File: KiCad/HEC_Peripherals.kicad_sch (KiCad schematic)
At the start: 17 parts, among them J2 Conn_02x12_Odd_Even, J6 DE9_Plug_MountingHoles, J7 AudioJack3, J8 NES_Port_Male, U43 74LS06, U44 74LS541, Y1 Crystal

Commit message: Preliminary routing
Changed footprint pad size to allow 2 traces to be routed between adjacent pads. Finished routing all ICs. Bypass caps not added. Some traces may need to be optimized.
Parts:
- U42: footprint Package_DIP:DIP-40_W15.24mm_Socket -> Library:DIP-40_W15.24mm_Socket_ThinPads
- U43: footprint Package_DIP:DIP-14_W7.62mm_Socket -> Library:DIP-14_W7.62mm_Socket_ThinPads
- U44: footprint Package_DIP:DIP-20_W7.62mm_Socket -> Library:DIP-20_W7.62mm_Socket_ThinPads
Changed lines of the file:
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@@
       (effects (font (size 1.27 1.27)))
     )
-    (property "Footprint" "Package_DIP:DIP-14_W7.62mm_Socket" (at 223.52 104.14 0)
+    (property "Footprint" "Library:DIP-14_W7.62mm_Socket_ThinPads" (at 223.52 104.14 0)
       (effects (font (size 1.27 1.27)) hide)
     )
@@
       (effects (font (size 1.27 1.27)))
     )
-    (property "Footprint" "Package_DIP:DIP-14_W7.62mm_Socket" (at 138.43 83.82 0)
+    (property "Footprint" "Library:DIP-14_W7.62mm_Socket_ThinPads" (at 138.43 83.82 0)
       (effects (font (size 1.27 1.27)) hide)
     )
@@
       (effects (font (size 1.27 1.27)))
     )
-    (property "Footprint" "Package_DIP:DIP-14_W7.62mm_Socket" (at 223.52 91.44 0)
+    (property "Footprint" "Library:DIP-14_W7.62mm_Socket_ThinPads" (at 223.52 91.44 0)
       (effects (font (size 1.27 1.27)) hide)
     )
@@
       (effects (font (size 1.27 1.27)) (justify left))
     )
-    (property "Footprint" "Package_DIP:DIP-20_W7.62mm_Socket" (at 94.615 167.64 0)
+    (property "Footprint" "Library:DIP-20_W7.62mm_Socket_ThinPads" (at 94.615 167.64 0)
       (effects (font (size 1.27 1.27)) hide)
     )
@@
       (effects (font (size 1.27 1.27)))
     )
-    (property "Footprint" "Package_DIP:DIP-14_W7.62mm_Socket" (at 223.52 65.405 0)
+    (property "Footprint" "Library:DIP-14_W7.62mm_Socket_ThinPads" (at 223.52 65.405 0)
       (effects (font (size 1.27 1.27)) hide)
     )
@@
       (effects (font (size 1.27 1.27)) (justify right))
     )
-    (property "Footprint" "Package_DIP:DIP-14_W7.62mm_Socket" (at 217.805 135.89 0)
+    (property "Footprint" "Library:DIP-14_W7.62mm_Socket_ThinPads" (at 217.805 135.89 0)
       (effects (font (size 1.27 1.27)) hide)
     )
@@
       (effects (font (size 1.27 1.27)))
     )
-    (property "Footprint" "Package_DIP:DIP-14_W7.62mm_Socket" (at 138.43 68.58 0)
+    (property "Footprint" "Library:DIP-14_W7.62mm_Socket_ThinPads" (at 138.43 68.58 0)
       (effects (font (size 1.27 1.27)) hide)
     )
@@
       (effects (font (size 1.27 1.27)))
     )
-    (property "Footprint" "Package_DIP:DIP-40_W15.24mm_Socket" (at 170.815 76.2 0)
+    (property "Footprint" "Library:DIP-40_W15.24mm_Socket_ThinPads" (at 170.815 76.2 0)
       (effects (font (size 1.27 1.27)) hide)
     )
@@
       (effects (font (size 1.27 1.27)))
     )
-    (property "Footprint" "Package_DIP:DIP-14_W7.62mm_Socket" (at 223.52 78.74 0)
-      (effects (font (size 1.27 1.27)) hide)
-    )
+    (property "Footprint" "Library:DIP-14_W7.62mm_Socket_ThinPads" (at 223.52 78.74 0)
+      (effects (font (size 1.27 1.27)) hide)
+    )

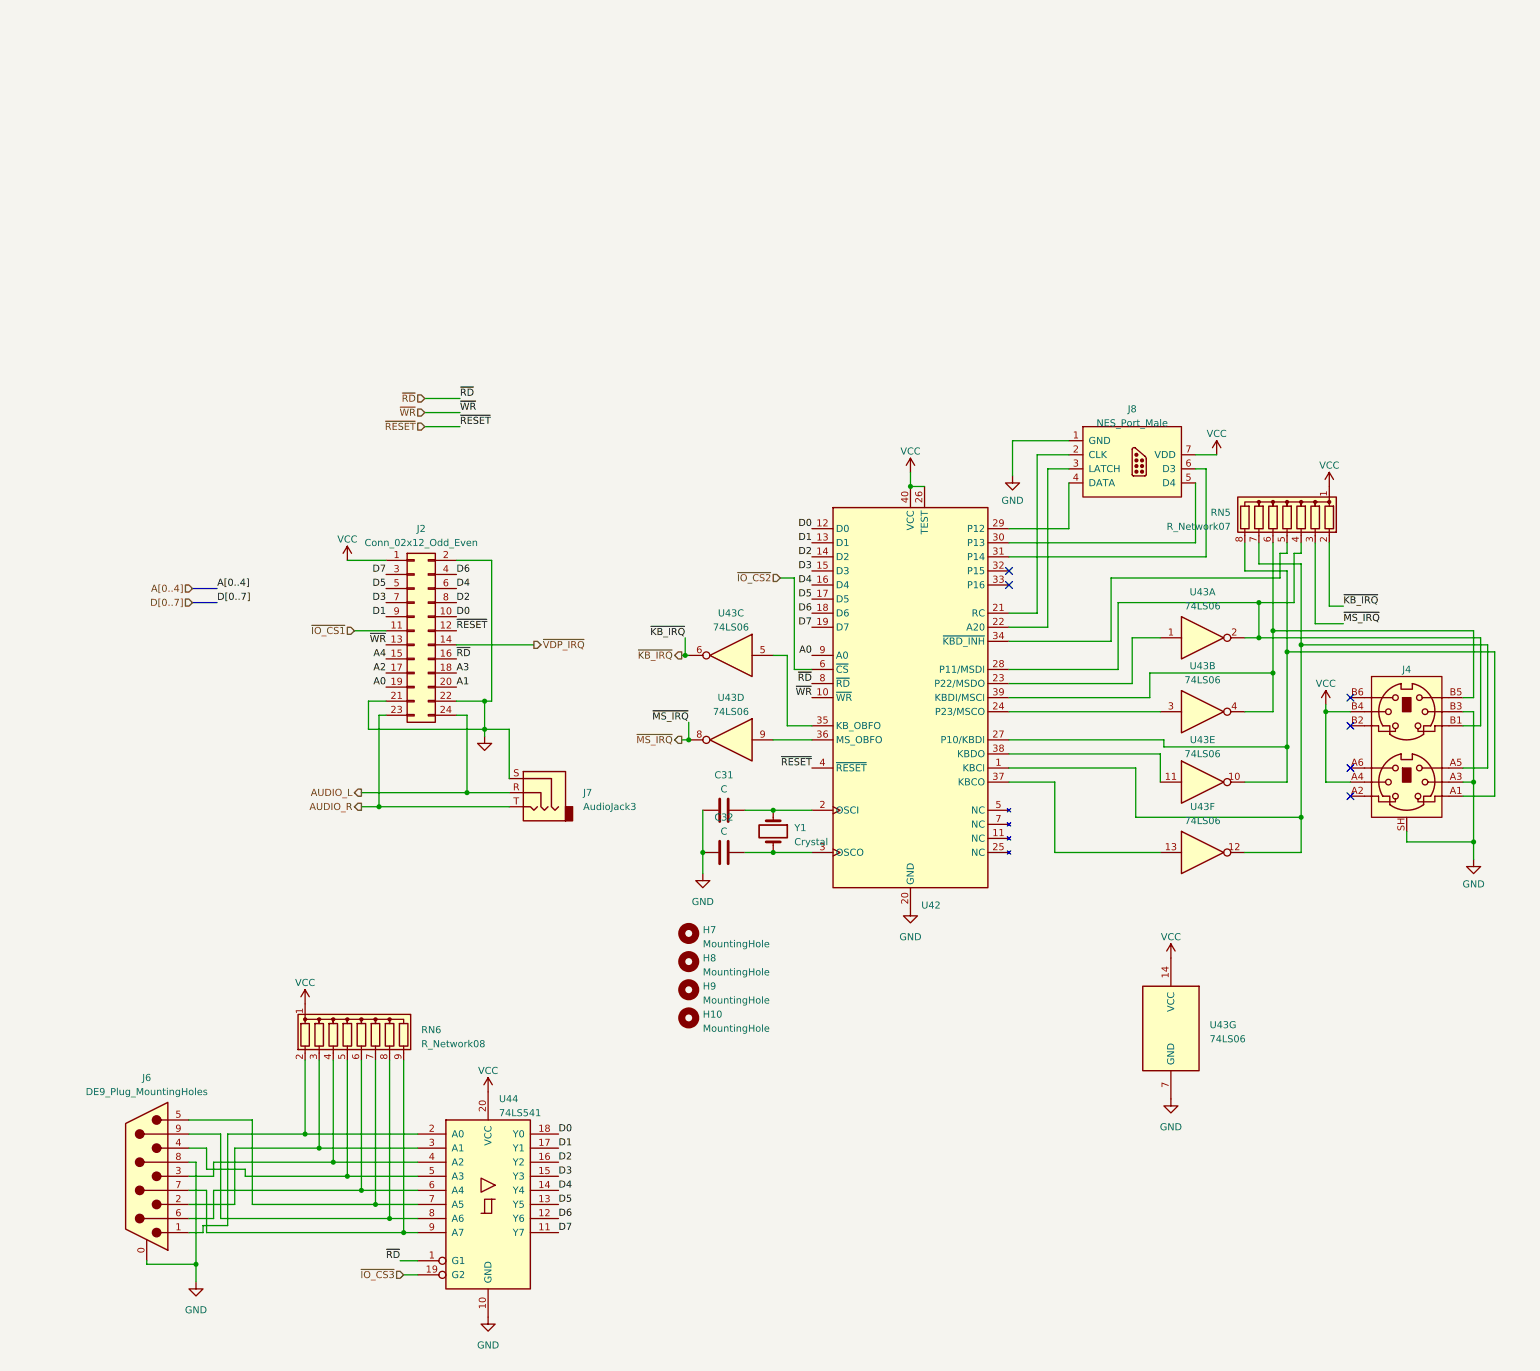
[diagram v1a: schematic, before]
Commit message: Change resistor network, add revision number
Changed most of the resistor network footprints so that they would accept both 9 pin and 5 pin resistor networks (since I bought 50 of those 5 pin ones!). Power routing optimizations. Added a revision number to the silkscreen to distinguish the board
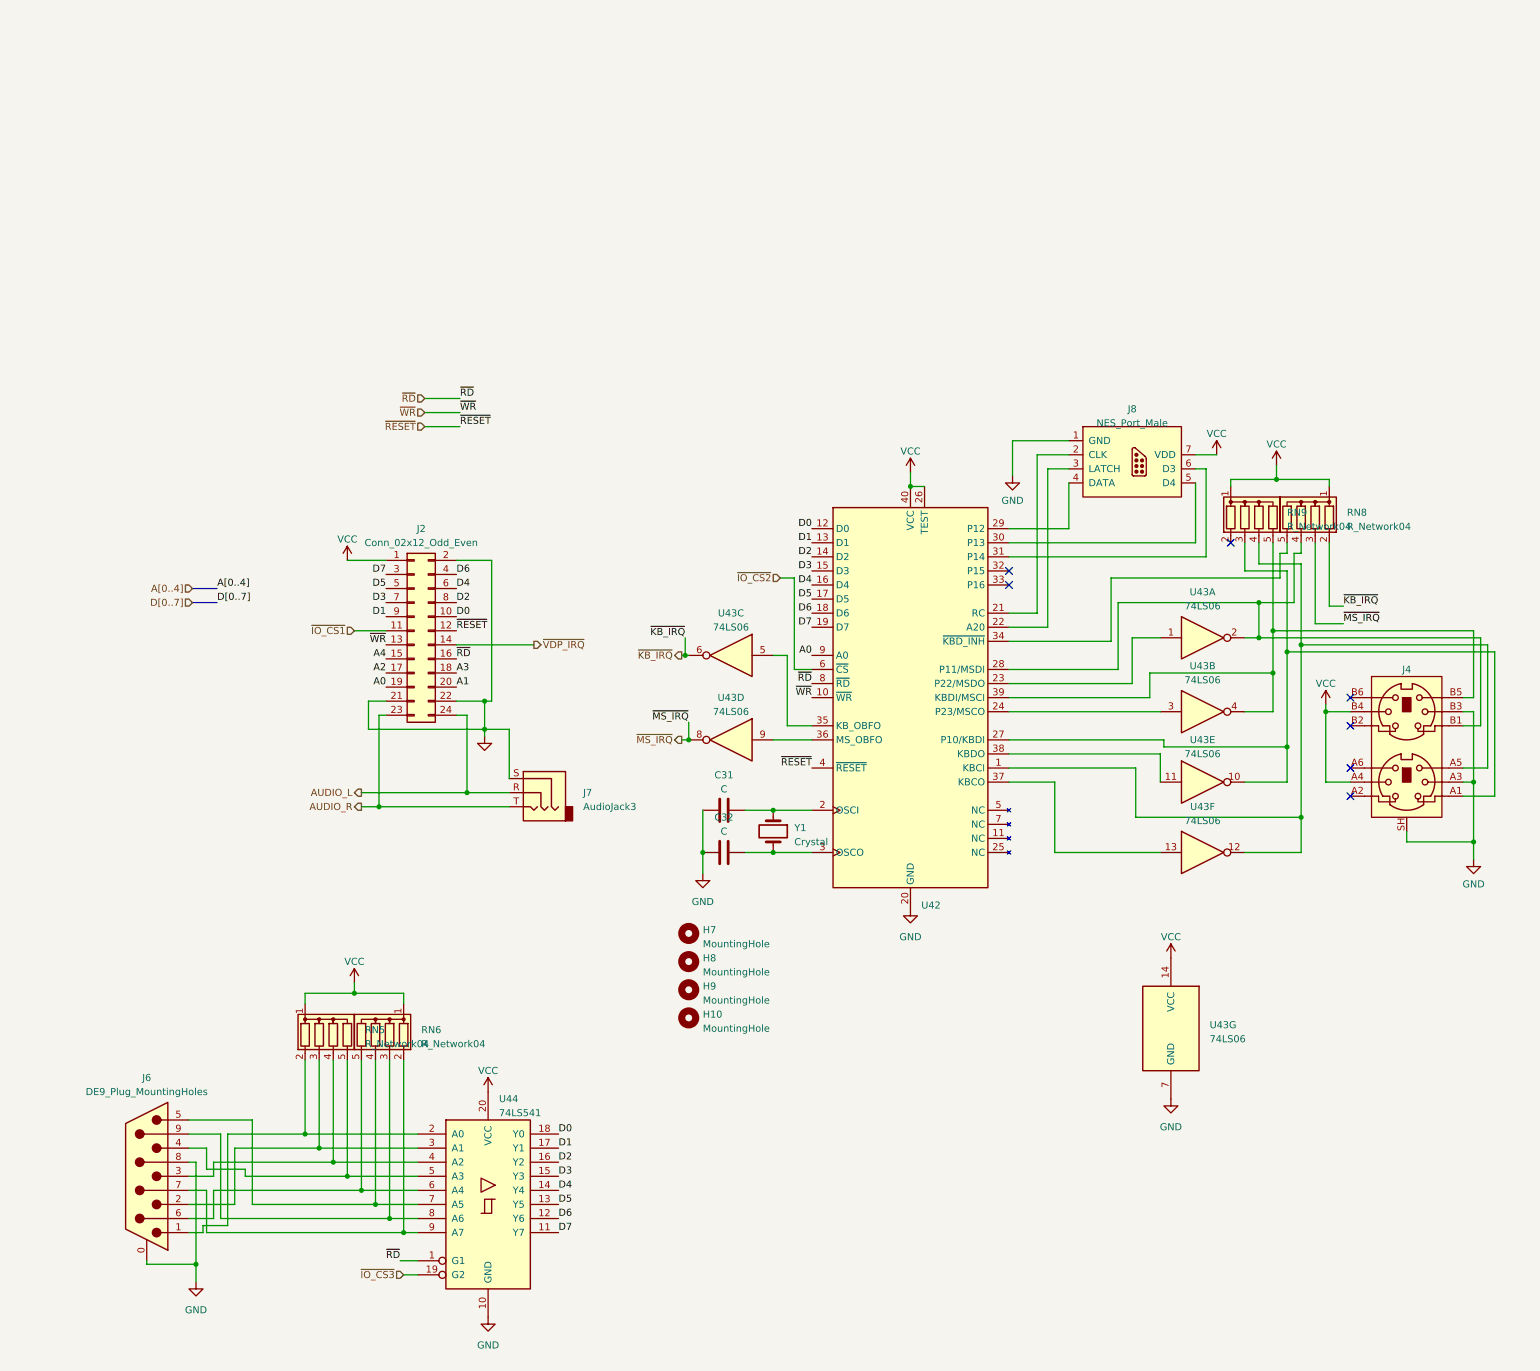
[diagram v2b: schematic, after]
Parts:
- removed RN5: R_Network07, Resistor_THT:R_Array_SIP8, symbol Device:R_Network07
- removed RN6: R_Network08, Resistor_THT:R_Array_SIP9, symbol Device:R_Network08
- added RN5, RN6, RN8, RN9: R_Network04, Resistor_THT:R_Array_SIP5, symbol Device:R_Network04
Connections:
- net VCC: now also RN5.1 (common), RN6.1 (common), RN8.1 (common), RN9.1 (common)
- net ~{KB_IRQ}: now also RN8.2 (R1)
- net ~{MS_IRQ}: now also RN8.3 (R2)
- net at J4.A1, U42.27 (P10/KBDI), U43.10: now also RN9.3 (R2)
- net at J4.A5, U42.1 (KBCI), U43.12: now also RN9.4 (R3)
- net at J4.B1, U42.28 (P11/MSDI), U43.2: now also RN8.4 (R3)
- net at J4.B5, U42.39 (KBDI/MSCI), U43.4: now also RN9.5 (R4)
- net at J6.1, U44.2 (A0): now also RN5.2 (R1)
- net at J6.2, U44.3 (A1): now also RN5.3 (R2)
- net at J6.3, U44.4 (A2): now also RN5.4 (R3)
- net at J6.4, U44.5 (A3): now also RN5.5 (R4)
- net at J6.6, U44.6 (A4): now also RN6.5 (R4)
- net at J6.5, U44.7 (A5): now also RN6.4 (R3)
- net at J6.9, U44.8 (A6): now also RN6.3 (R2)
- net at J6.7, U44.9 (A7): now also RN6.2 (R1)
- net at U42.34 (~{KBD_INH}): now also RN8.5 (R4)
- no-connect marks 6 -> 7

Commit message: Updates to circuit
Updates to the second gen circuit
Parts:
- added J9: Conn_02x05_Odd_Even, symbol Connector_Generic:Conn_02x05_Odd_Even
- added NT31, NT32: NetTie_2, symbol Device:NetTie_2
- added U47: TL074, symbol Amplifier_Operational:TL074
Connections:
- net GND: now also NT31.1, NT32.1; no longer J7.S
- net AUDIO_L renamed VERA_L
- net VERA_L: no longer J7.R
- net AUDIO_R renamed VERA_R
- net VERA_R: no longer J7.T
- new net: J7.S, NT32.2
- new net: J9.2 (Pin_2), NT31.2
- new net audiojack_L: J7.R
- new net audiojack_R: J7.T
- new net header_L: J9.9 (Pin_9)
- new net header_R: J9.5 (Pin_5)
- no-connect marks 7 -> 14
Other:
- moved on the sheet: H10, H7, H8, H9, J2, RN5, RN6, U43G
